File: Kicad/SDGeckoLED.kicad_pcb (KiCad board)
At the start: 2 copper layers, 30 x 30.5 mm, 8 parts, among them J4 MICRO-SD-CARD, U1 74AHC1G32

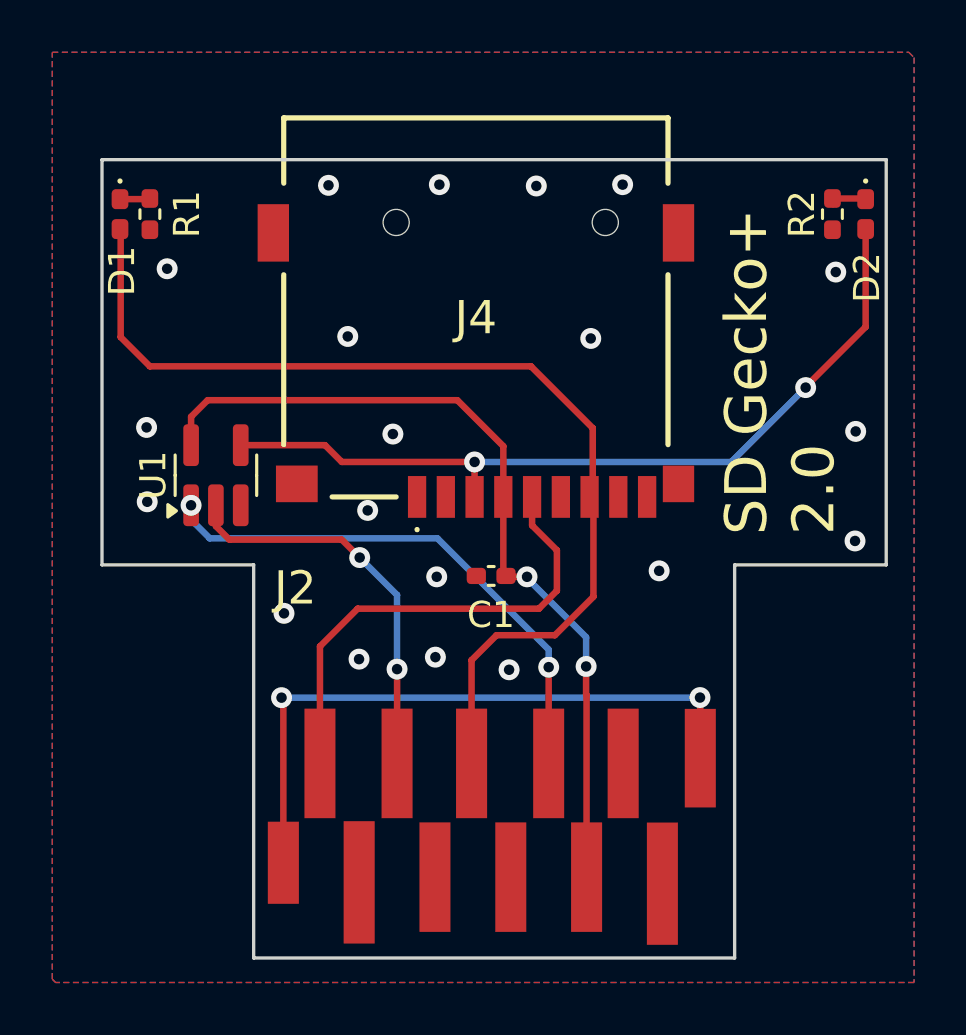
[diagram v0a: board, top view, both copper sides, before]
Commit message: updated kicad project for sd gerber fix
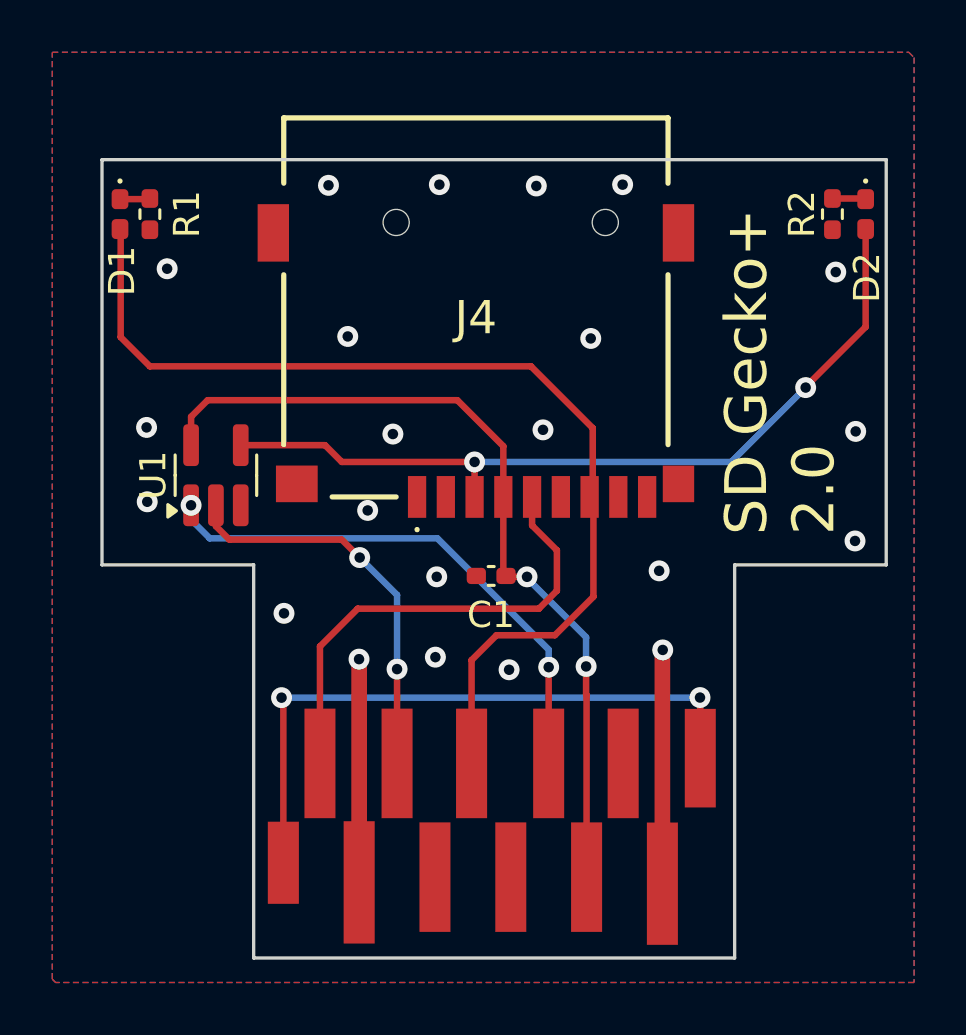
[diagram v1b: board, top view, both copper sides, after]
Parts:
- R1, R2: value 10R -> 14R
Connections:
- J4 pad G1: GND -> unconnected-(J4-GND-PadG1)
- J4 pad MP1: GND -> unconnected-(J4-PadMP1)
- J4 pad MP2: GND -> unconnected-(J4-PadMP2)
- J4 pad MP3: GND -> unconnected-(J4-PadMP3)
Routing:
- net GND: track 0.46 -> 17.5 mm, vias 20 -> 22
